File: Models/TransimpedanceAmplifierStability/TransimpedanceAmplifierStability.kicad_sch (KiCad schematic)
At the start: 1 part

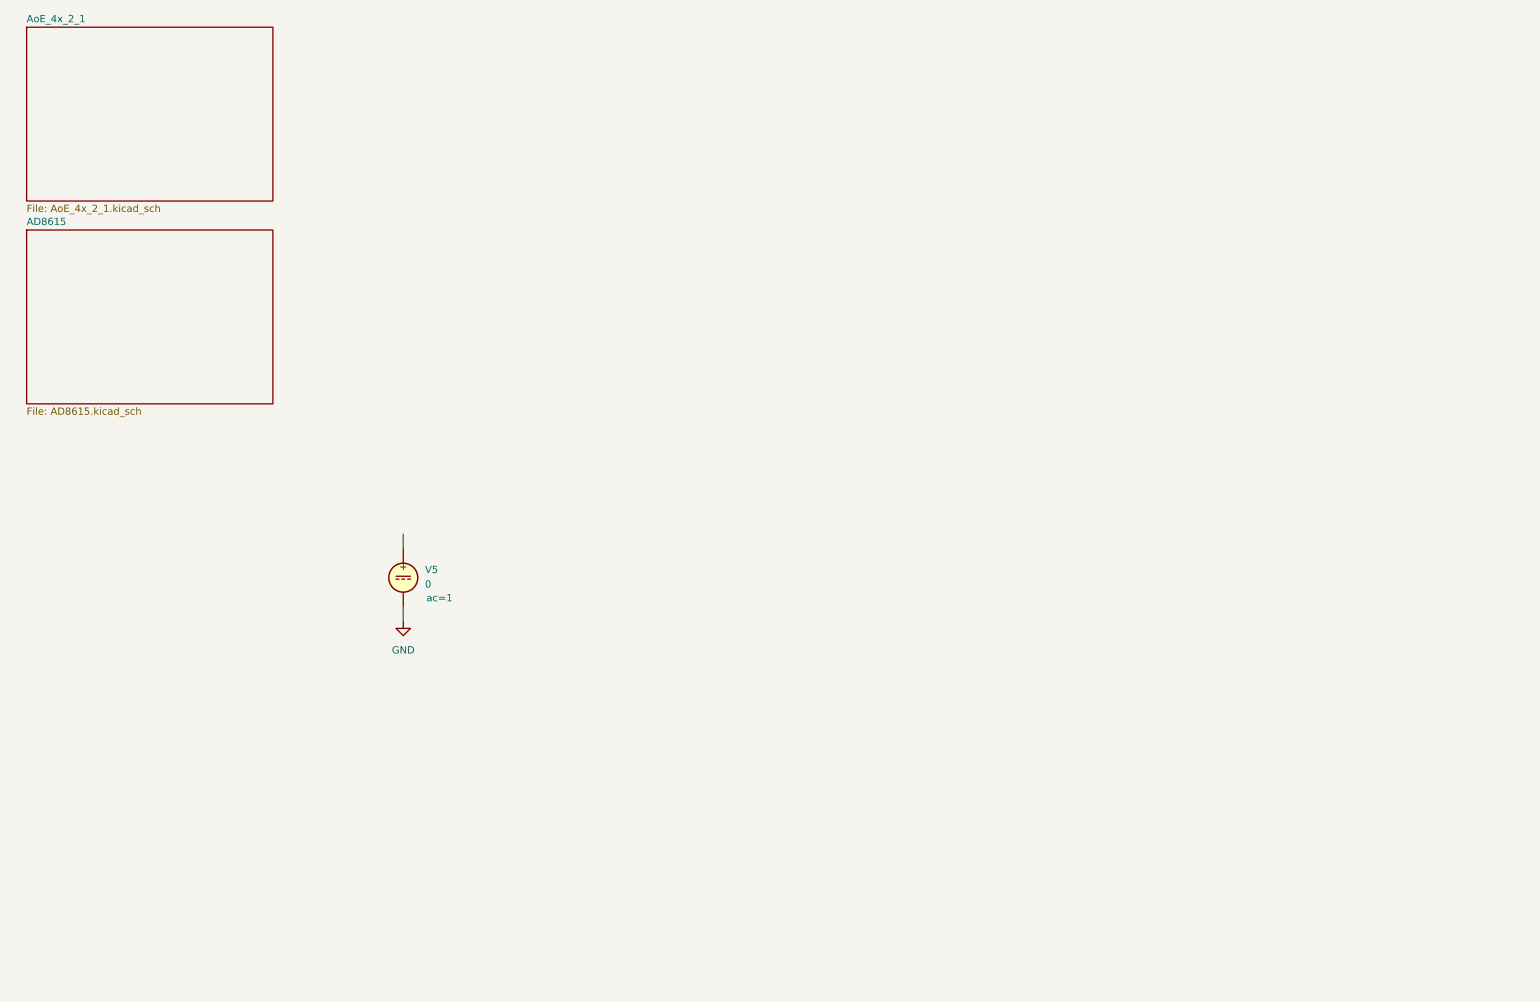
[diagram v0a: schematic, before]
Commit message: Add the Bode plot of the OP37G
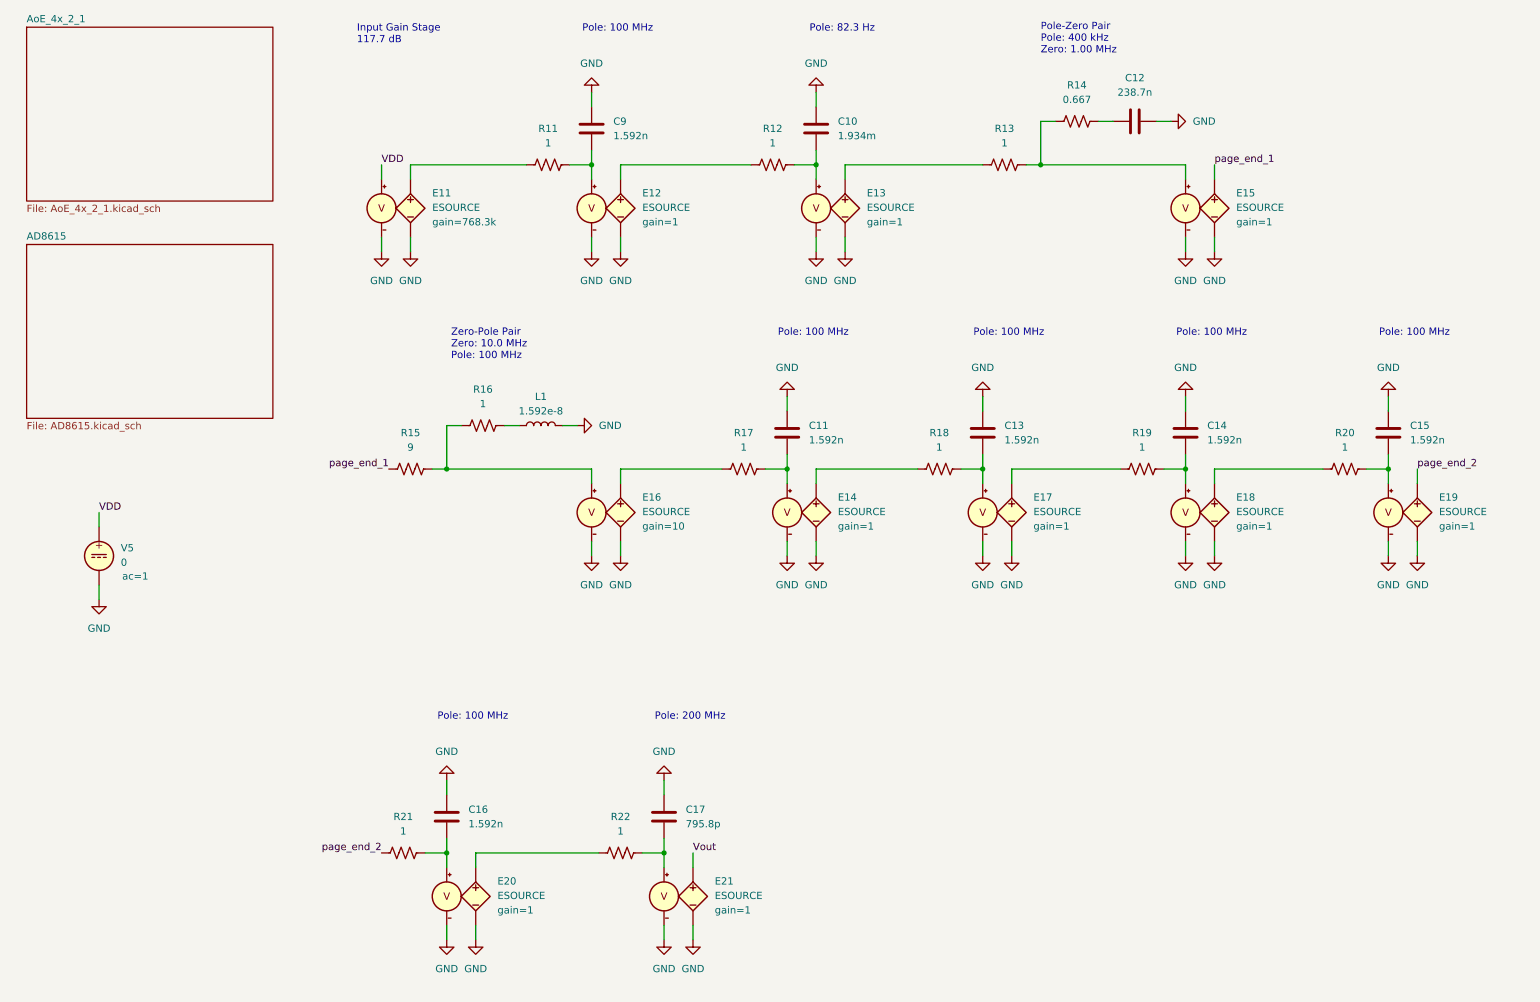
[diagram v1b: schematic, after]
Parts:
- added C10: 1.934m, symbol Device:C
- added C11, C13, C14, C15, C16, C9: 1.592n, symbol Device:C
- added C12: 238.7n, symbol Device:C
- added C17: 795.8p, symbol Device:C
- added E11, E12, E13, E14, E15, E16, E17, E18, E19, E20, E21: ESOURCE, symbol Simulation_SPICE:ESOURCE
- added L1: 1.592e-8, symbol Device:L
- added R11, R12, R13, R16, R17, R18, R19, R20, R21, R22: 1, symbol Device:R_US
- added R14: 0.667, symbol Device:R_US
- added R15: 9, symbol Device:R_US
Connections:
- net GND: now also C10.1, C11.1, C12.1, C13.1, C14.1, C15.1, C16.1, C17.1, C9.1, E11.2 (N-), E11.4 (C-), E12.2 (N-), E12.4 (C-), E13.2 (N-), E13.4 (C-), E14.2 (N-), E14.4 (C-), E15.2 (N-), E15.4 (C-), E16.2 (N-), E16.4 (C-), E17.2 (N-), E17.4 (C-), E18.2 (N-), E18.4 (C-), E19.2 (N-), E19.4 (C-), E20.2 (N-), E20.4 (C-), E21.2 (N-), E21.4 (C-), L1.2
- net VDD: now reaches V5.1
- net VDD: now also E11.3 (C+)
- new net: E16.1 (N+), R17.1
- new net: C11.2, E14.3 (C+), R17.2
- new net: C9.2, E12.3 (C+), R11.2
- new net: C15.2, E19.3 (C+), R20.2
- new net: E18.1 (N+), R20.1
- new net: C14.2, E18.3 (C+), R19.2
- new net: E11.1 (N+), R11.1
- new net: C13.2, E17.3 (C+), R18.2
- new net: E12.1 (N+), R12.1
- new net: C10.2, E13.3 (C+), R12.2
- new net: C16.2, E20.3 (C+), R21.2
- new net: E16.3 (C+), R15.2, R16.2
- new net: E15.3 (C+), R13.2, R14.2
- new net: L1.1, R16.1
- new net: E13.1 (N+), R13.1
- new net: E14.1 (N+), R18.1
- new net: E20.1 (N+), R22.1
- new net: C12.2, R14.1
- new net: E17.1 (N+), R19.1
- new net: C17.2, E21.3 (C+), R22.2
- new net Vout: E21.1 (N+)
- new net page_end_1: E15.1 (N+), R15.1
- new net page_end_2: E19.1 (N+), R21.1
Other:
- note added: "Input Gain Stage 117.7 dB"
- note added: "Pole-Zero Pair Pole: 400 kHz Zero: 1.00 MHz"
- note added: "Pole: 100 MHz"
- note added: "Pole: 200 MHz"
- note added: "Pole: 82.3 Hz"
- note added: "Zero-Pole Pair Zero: 10.0 MHz Pole: 100 MHz"
- moved on the sheet: V5

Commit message: Upload completed model of the LTC6090-5
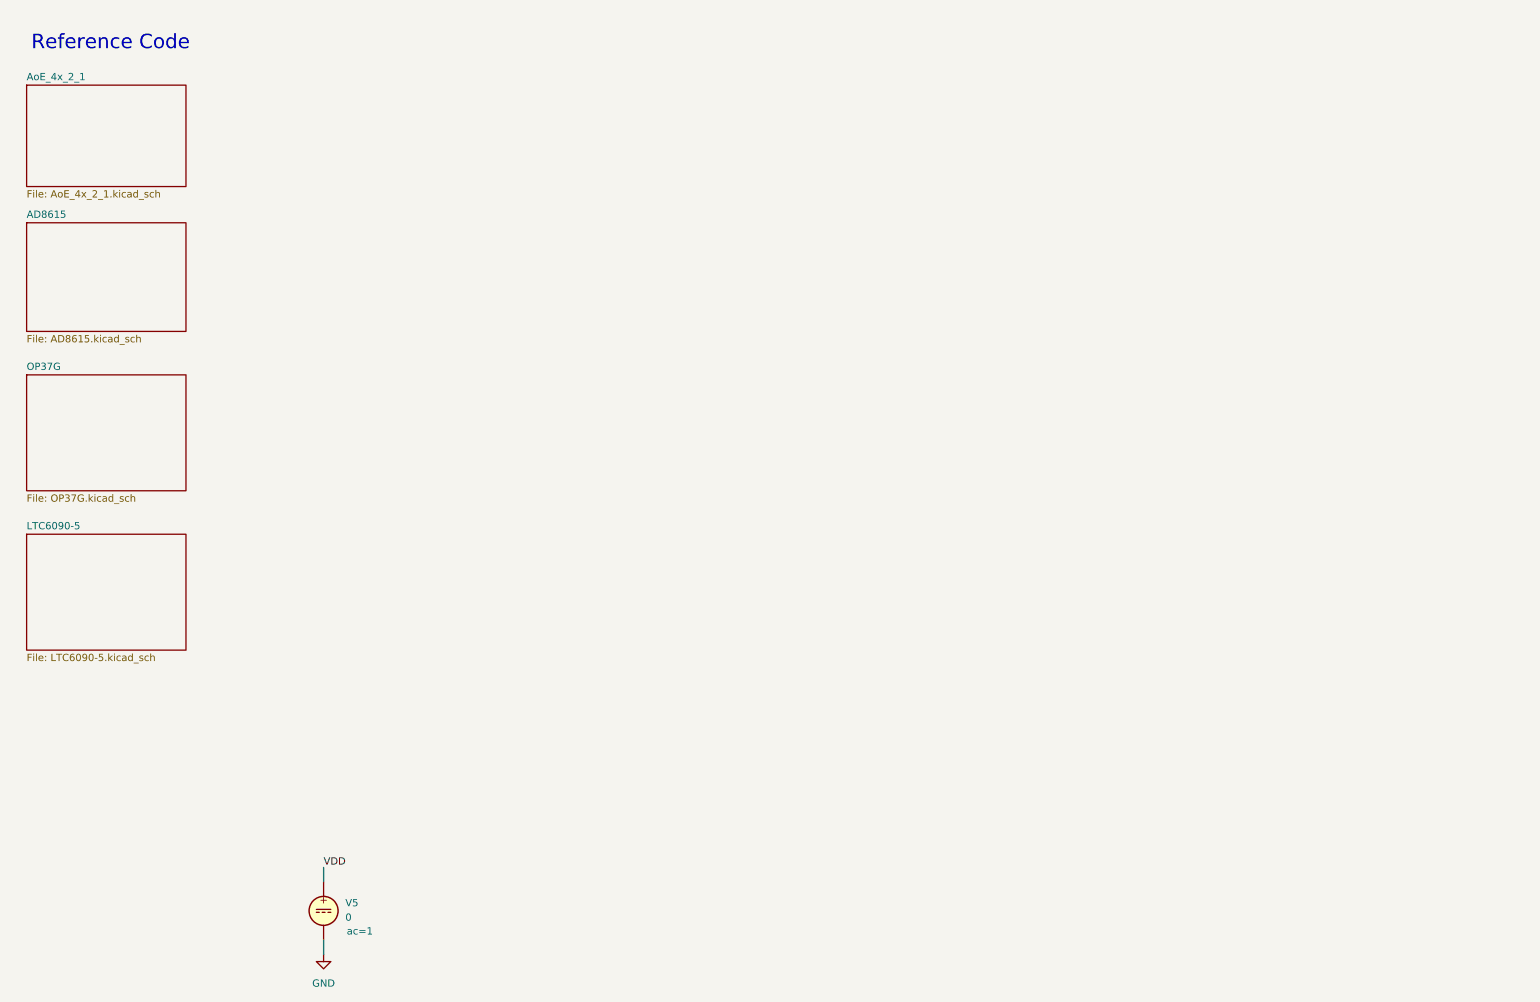
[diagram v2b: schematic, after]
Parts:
- removed C10: 1.934m, symbol Device:C
- removed C11, C13, C14, C15, C16, C9: 1.592n, symbol Device:C
- removed C12: 238.7n, symbol Device:C
- removed C17: 795.8p, symbol Device:C
- removed E11, E12, E13, E14, E15, E16, E17, E18, E19, E20, E21: ESOURCE, symbol Simulation_SPICE:ESOURCE
- removed L1: 1.592e-8, symbol Device:L
- removed R11, R12, R13, R16, R17, R18, R19, R20, R21, R22: 1, symbol Device:R_US
- removed R14: 0.667, symbol Device:R_US
- removed R15: 9, symbol Device:R_US
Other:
- added sheet LTC6090-5 (LTC6090-5.kicad_sch)
- added sheet OP37G (OP37G.kicad_sch)
- note added: "Reference Code"
- note removed: "Input Gain Stage 117.7 dB"
- note removed: "Pole-Zero Pair Pole: 400 kHz Zero: 1.00 MHz"
- note removed: "Pole: 100 MHz"
- note removed: "Pole: 200 MHz"
- note removed: "Pole: 82.3 Hz"
- note removed: "Zero-Pole Pair Zero: 10.0 MHz Pole: 100 MHz"
- moved on the sheet: V5

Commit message: Upload latest version of TIA stability KiCad project
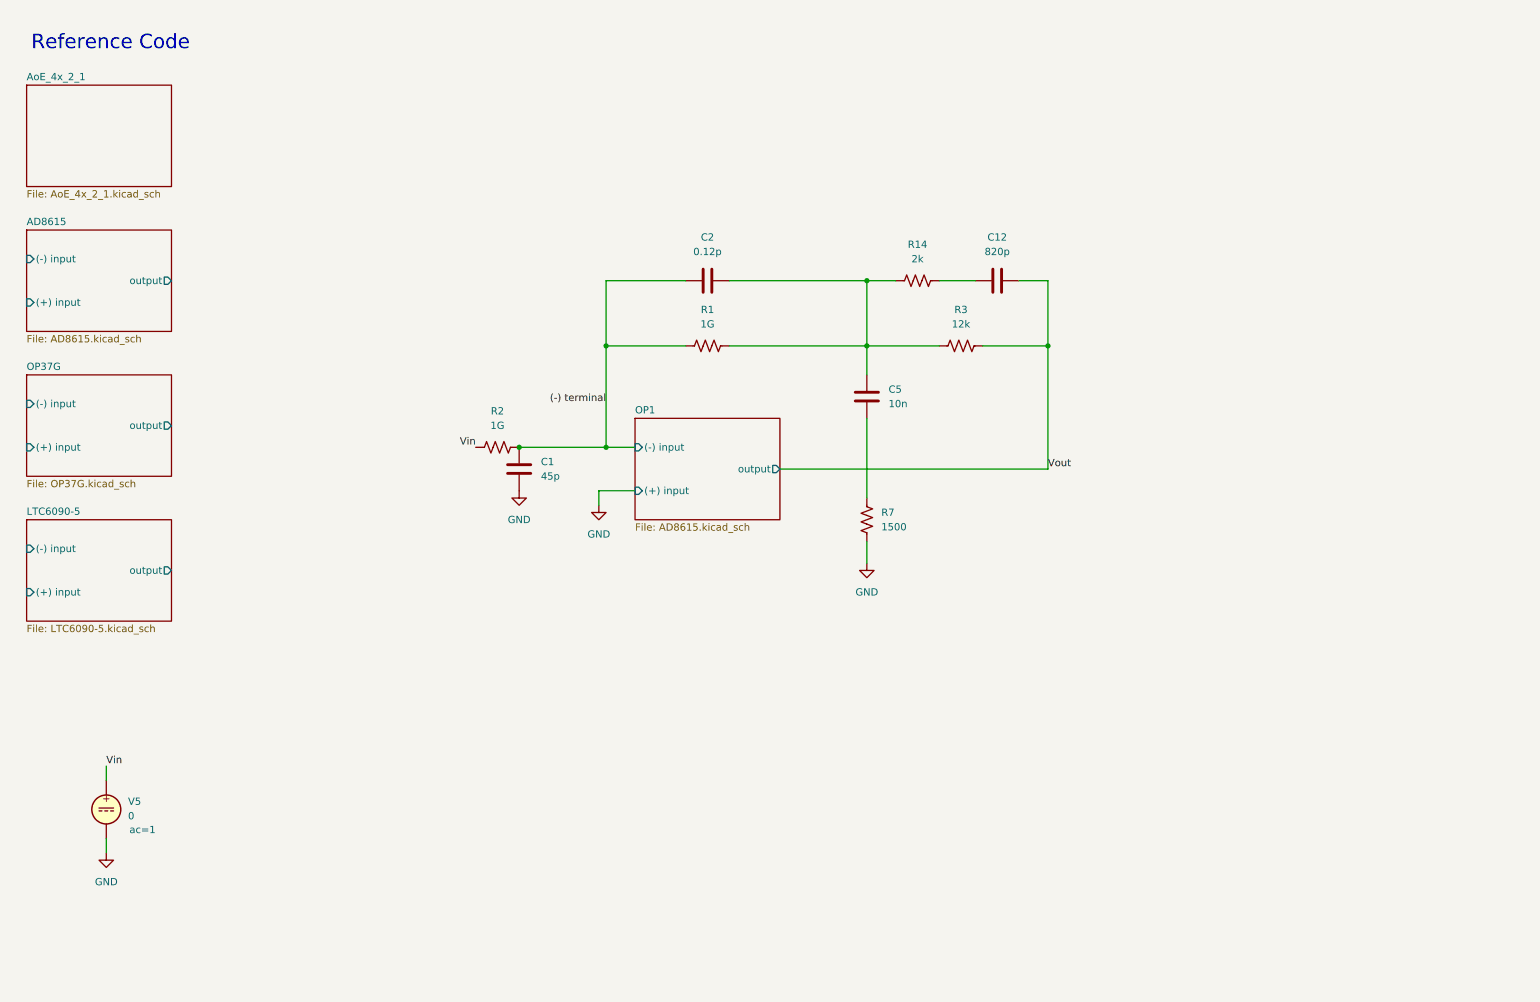
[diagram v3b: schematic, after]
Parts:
- added C1: 45p, symbol Device:C
- added C12: 820p, symbol Device:C
- added C2: 0.12p, symbol Device:C
- added C5: 10n, symbol Device:C
- added R1, R2: 1G, symbol Device:R_US
- added R14: 2k, symbol Device:R_US
- added R3: 12k, symbol Device:R_US
- added R7: 1500, symbol Device:R_US
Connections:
- net GND: now also C1.2, R7.2
- net VDD renamed Vin
- net Vin: now also R2.1
- new net: C2.2, C5.1, R1.2, R14.1, R3.1
- new net: C5.2, R7.1
- new net: C12.1, R14.2
- new net (-) terminal: C1.1, C2.1, R1.1, R2.2
- new net Vout: C12.2, R3.2
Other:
- added sheet OP1 (AD8615.kicad_sch)
- sheet AD8615 ports: added (+) input, (-) input, output; removed none
- sheet LTC6090-5 ports: added (+) input, (-) input, output; removed none
- sheet OP37G ports: added (+) input, (-) input, output; removed none
- moved on the sheet: V5

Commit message: Upload KiCad project with fully developed model of TIA from the paper
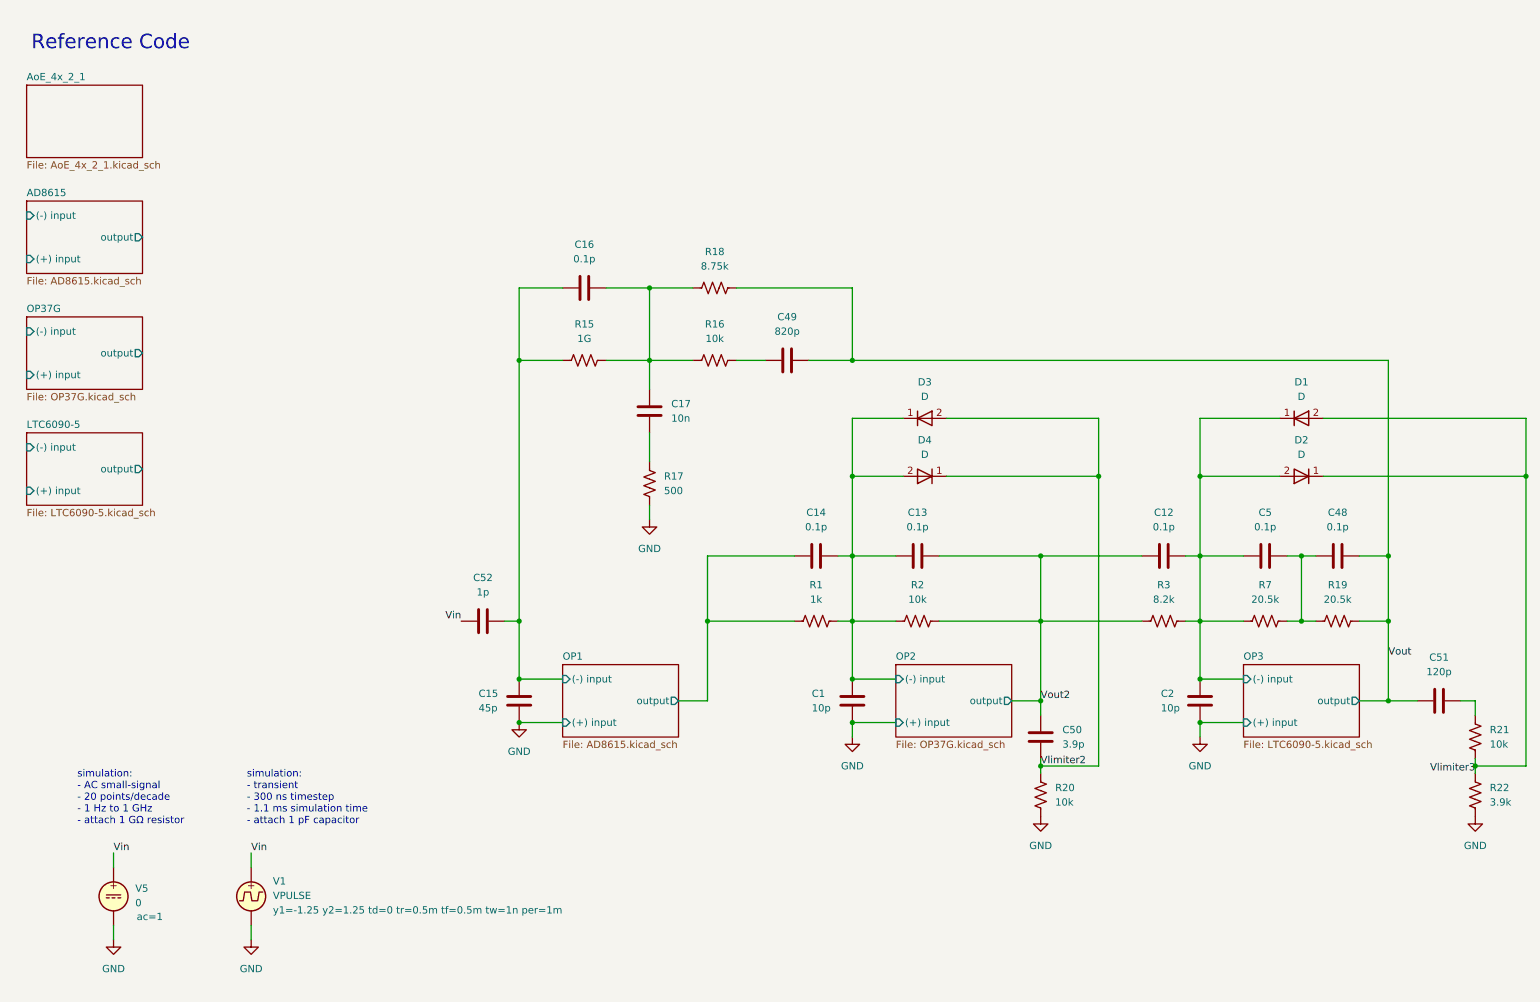
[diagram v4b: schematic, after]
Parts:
- removed R14: 2k, symbol Device:R_US
- added C13, C14, C16, C48: 0.1p, symbol Device:C
- added C15: 45p, symbol Device:C
- added C17: 10n, symbol Device:C
- added C49: 820p, symbol Device:C
- added C50: 3.9p, symbol Device:C
- added C51: 120p, symbol Device:C
- added C52: 1p, symbol Device:C
- added D1, D2, D3, D4: D, symbol Simulation_SPICE:D
- added R15: 1G, symbol Device:R_US
- added R16, R20, R21: 10k, symbol Device:R_US
- added R17: 500, symbol Device:R_US
- added R18: 8.75k, symbol Device:R_US
- added R19: 20.5k, symbol Device:R_US
- added R22: 3.9k, symbol Device:R_US
- added V1: VPULSE, symbol Simulation_SPICE:VPULSE
- C1: value 45p -> 10p
- C12: value 820p -> 0.1p
- C2: value 0.12p -> 10p
- C5: value 10n -> 0.1p
- R1: value 1G -> 1k
- R2: value 1G -> 10k
- R3: value 12k -> 8.2k
- R7: value 1500 -> 20.5k
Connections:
- net GND: now also C2.2, C15.2, R17.2, R20.2, R22.2, V1.2; no longer R7.2
- net Vin: now also C52.1, V1.1; no longer R2.1
- net Vout: now also C48.2, C49.2, C51.2, R18.2, R19.2; no longer C12.2, R3.2
- net at C5.2: now also R7.2, C48.1, R19.1; no longer R7.1
- net Vout2: now reaches C12.1
- net Vout2: now also R2.2, R3.1, C13.2, C50.1
- removed net (-) terminal: C1.1, C2.1, R1.1, R2.2
- new net: C51.1, R21.1
- new net: C49.1, R16.2
- new net: C16.2, C17.1, R15.2, R16.1, R18.1
- new net: C17.2, R17.1
- new net OP1/(-) input: C15.1, C16.1, C52.2, R15.1
- new net OP1/output: C14.1, R1.1
- new net OP2/(-) input: C1.1, C13.1, C14.2, D3.1 (K), D4.2 (A), R1.2, R2.1
- new net OP3/(-) input: C12.2, C2.1, C5.1, D1.1 (K), D2.2 (A), R3.2, R7.1
- new net Vlimiter2: C50.2, D3.2 (A), D4.1 (K), R20.1
- new net Vlimiter3: D1.2 (A), D2.1 (K), R21.2, R22.1
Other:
- added sheet OP2 (OP37G.kicad_sch)
- added sheet OP3 (LTC6090-5.kicad_sch)
- note added: "simulation: - AC small-signal - 20 points/decade - 1 Hz to 1 GHz - attach 1 GΩ resistor"
- note added: "simulation: - transient - 300 ns timestep - 1.1 ms simulation time - attach 1 pF capacitor"
- moved on the sheet: V5
